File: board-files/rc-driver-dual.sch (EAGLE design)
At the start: 18 parts

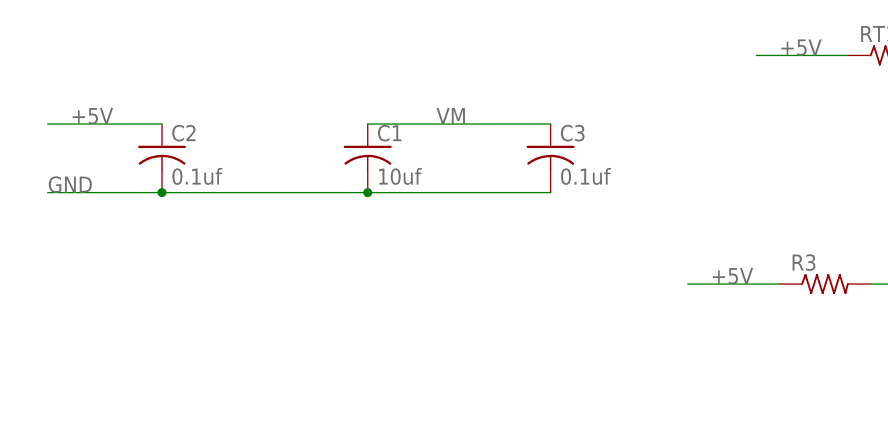
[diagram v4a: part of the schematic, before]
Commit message: Move squigly lines and extra capacitance on VM.
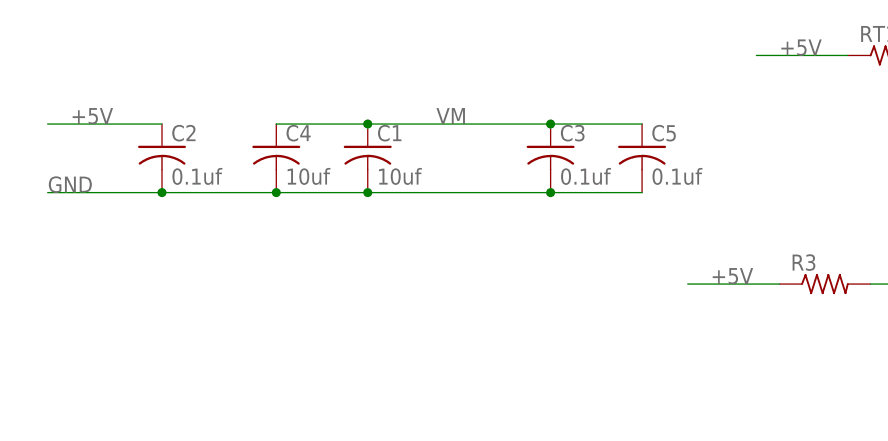
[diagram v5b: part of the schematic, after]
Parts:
- added C4: 10uf, resistor:C-USC1206
- added C5: 0.1uf, resistor:C-USC0603
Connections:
- net GND: now also C4.2, C5.2
- net VM: now also C4.1, C5.1
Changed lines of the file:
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@@
 <part name="R6" library="resistor" deviceset="R-US_" device="R0603"/>
 <part name="LED2" library="led" deviceset="LED" device="CHIPLED_0603"/>
+<part name="C4" library="resistor" deviceset="C-US" device="C1206" value="10uf"/>
+<part name="C5" library="resistor" deviceset="C-US" device="C0603" value="0.1uf"/>
 </parts>
 <sheets>
@@
 <instance part="R6" gate="G$1" x="93.98" y="40.64"/>
 <instance part="LED2" gate="G$1" x="109.22" y="40.64" rot="R90"/>
+<instance part="C4" gate="G$1" x="12.7" y="116.84"/>
+<instance part="C5" gate="G$1" x="53.34" y="116.84"/>
 </instances>
 <busses>
@@
 <pinref part="C1" gate="G$1" pin="1"/>
 <label x="30.48" y="119.38" size="1.778" layer="95"/>
+<pinref part="C4" gate="G$1" pin="1"/>
+<wire x1="12.7" y1="119.38" x2="22.86" y2="119.38" width="0.1524" layer="91"/>
+<pinref part="C5" gate="G$1" pin="1"/>
+<wire x1="43.18" y1="119.38" x2="53.34" y2="119.38" width="0.1524" layer="91"/>
+<junction x="43.18" y="119.38"/>
+<junction x="22.86" y="119.38"/>
 </segment>
 <segment>
@@
 <pinref part="C2" gate="G$1" pin="2"/>
 <wire x1="0" y1="111.76" x2="-12.7" y2="111.76" width="0.1524" layer="91"/>
-<wire x1="22.86" y1="111.76" x2="0" y2="111.76" width="0.1524" layer="91"/>
+<wire x1="22.86" y1="111.76" x2="12.7" y2="111.76" width="0.1524" layer="91"/>
 <label x="-12.7" y="111.76" size="1.778" layer="95"/>
 <junction x="22.86" y="111.76"/>
 <junction x="0" y="111.76"/>
+<pinref part="C4" gate="G$1" pin="2"/>
+<wire x1="12.7" y1="111.76" x2="0" y2="111.76" width="0.1524" layer="91"/>
+<junction x="12.7" y="111.76"/>
+<pinref part="C5" gate="G$1" pin="2"/>
+<wire x1="43.18" y1="111.76" x2="53.34" y2="111.76" width="0.1524" layer="91"/>
+<junction x="43.18" y="111.76"/>
 </segment>
 <segment>

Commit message: Moving single board files to different folder.
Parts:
- R3: value (none) -> 5600
- R4: value (none) -> 1300
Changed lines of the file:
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@@
 <part name="R1" library="resistor" deviceset="R-US_" device="R0805W"/>
 <part name="R2" library="resistor" deviceset="R-US_" device="R0805W"/>
-<part name="R3" library="resistor" deviceset="R-US_" device="R0603"/>
-<part name="R4" library="resistor" deviceset="R-US_" device="R0603"/>
+<part name="R3" library="resistor" deviceset="R-US_" device="R0603" value="5600"/>
+<part name="R4" library="resistor" deviceset="R-US_" device="R0603" value="1300"/>
 <part name="R5" library="resistor" deviceset="R-US_" device="R0603"/>
 <part name="LED1" library="led" deviceset="LED" device="CHIPLED_0603"/>

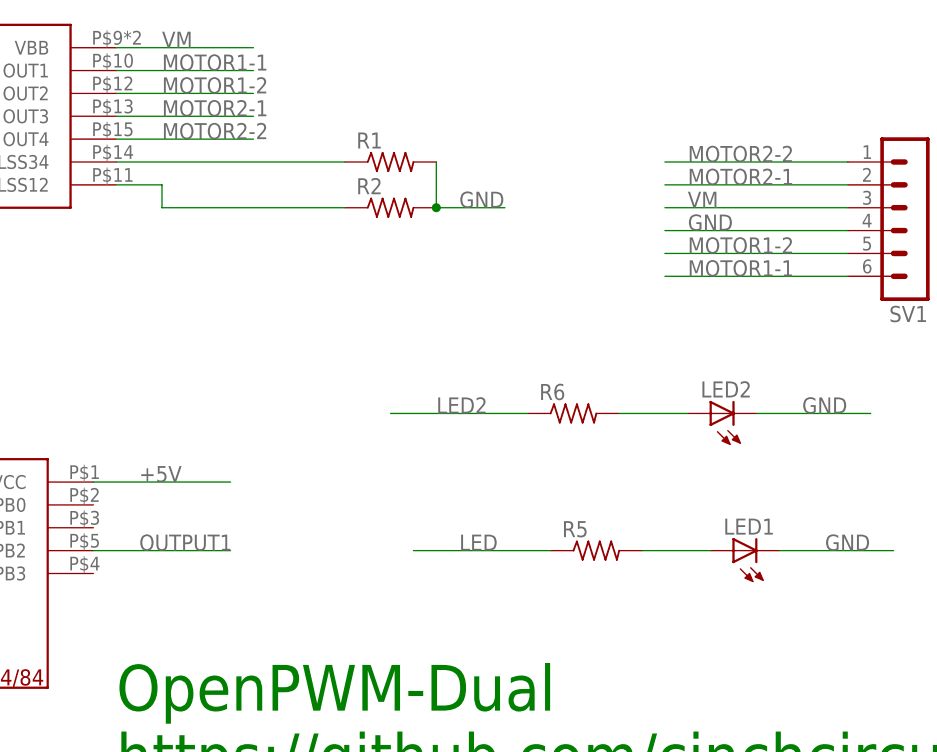
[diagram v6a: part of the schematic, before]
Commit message: Changes for battlebot competition.   More part information.   Changed steering and forward direction mixing.   Have one led for signal, and the other for no signal.
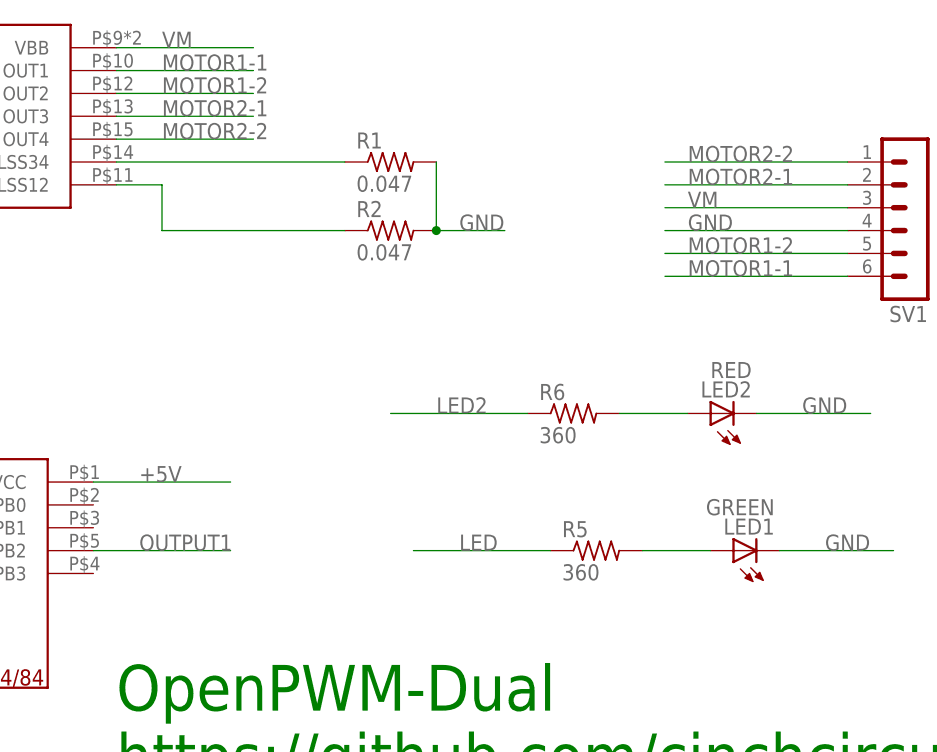
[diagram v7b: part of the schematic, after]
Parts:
- LED1: value (none) -> GREEN
- LED2: value (none) -> RED
- R1, R2: value (none) -> 0.047
- R5, R6: value (none) -> 360
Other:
- moved on the sheet: R2
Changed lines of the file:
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@@
 <part name="C2" library="resistor" deviceset="C-US" device="C0603" value="0.1uf"/>
 <part name="C3" library="resistor" deviceset="C-US" device="C0603" value="0.1uf"/>
-<part name="R1" library="resistor" deviceset="R-US_" device="R0805W"/>
-<part name="R2" library="resistor" deviceset="R-US_" device="R0805W"/>
+<part name="R1" library="resistor" deviceset="R-US_" device="R0805W" value="0.047"/>
+<part name="R2" library="resistor" deviceset="R-US_" device="R0805W" value="0.047"/>
 <part name="R3" library="resistor" deviceset="R-US_" device="R0603" value="5600"/>
 <part name="R4" library="resistor" deviceset="R-US_" device="R0603" value="1300"/>
-<part name="R5" library="resistor" deviceset="R-US_" device="R0603"/>
-<part name="LED1" library="led" deviceset="LED" device="CHIPLED_0603"/>
+<part name="R5" library="resistor" deviceset="R-US_" device="R0603" value="360"/>
+<part name="LED1" library="led" deviceset="LED" device="CHIPLED_0603" value="GREEN"/>
 <part name="RT1" library="resistor" deviceset="R-US_" device="R0603"/>
 <part name="R7" library="resistor" deviceset="R-US_" device="R0603"/>
-<part name="R6" library="resistor" deviceset="R-US_" device="R0603"/>
-<part name="LED2" library="led" deviceset="LED" device="CHIPLED_0603"/>
+<part name="R6" library="resistor" deviceset="R-US_" device="R0603" value="360"/>
+<part name="LED2" library="led" deviceset="LED" device="CHIPLED_0603" value="RED"/>
 <part name="C4" library="resistor" deviceset="C-US" device="C1206" value="10uf"/>
 <part name="C5" library="resistor" deviceset="C-US" device="C0603" value="0.1uf"/>
@@
 <instance part="C3" gate="G$1" x="43.18" y="116.84"/>
 <instance part="R1" gate="G$1" x="73.66" y="68.58"/>
-<instance part="R2" gate="G$1" x="73.66" y="63.5"/>
+<instance part="R2" gate="G$1" x="73.66" y="60.96"/>
 <instance part="R3" gate="G$1" x="73.66" y="101.6"/>
 <instance part="R4" gate="G$1" x="91.44" y="101.6"/>
@@
 <pinref part="R1" gate="G$1" pin="2"/>
 <pinref part="R2" gate="G$1" pin="2"/>
-<wire x1="78.74" y1="68.58" x2="78.74" y2="63.5" width="0.1524" layer="91"/>
-<wire x1="78.74" y1="63.5" x2="86.36" y2="63.5" width="0.1524" layer="91"/>
-<junction x="78.74" y="63.5"/>
-<label x="81.28" y="63.5" size="1.778" layer="95"/>
+<wire x1="78.74" y1="68.58" x2="78.74" y2="60.96" width="0.1524" layer="91"/>
+<wire x1="78.74" y1="60.96" x2="86.36" y2="60.96" width="0.1524" layer="91"/>
+<junction x="78.74" y="60.96"/>
+<label x="81.28" y="60.96" size="1.778" layer="95"/>
 </segment>
 <segment>
@@
 <segment>
 <pinref part="R2" gate="G$1" pin="1"/>
-<wire x1="68.58" y1="63.5" x2="48.26" y2="63.5" width="0.1524" layer="91"/>
-<wire x1="48.26" y1="63.5" x2="48.26" y2="66.04" width="0.1524" layer="91"/>
+<wire x1="68.58" y1="60.96" x2="48.26" y2="60.96" width="0.1524" layer="91"/>
+<wire x1="48.26" y1="60.96" x2="48.26" y2="66.04" width="0.1524" layer="91"/>
 <pinref part="U$2" gate="G$1" pin="LSS12"/>
 <wire x1="48.26" y1="66.04" x2="43.18" y2="66.04" width="0.1524" layer="91"/>
